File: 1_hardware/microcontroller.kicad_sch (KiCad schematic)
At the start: 42 parts, among them J1 ProgHeader, SW1 TS-1187A-B-A-B, SW2 TS-1187A-B-A-B, U1 STM32L151C8T6, X1 16MHz

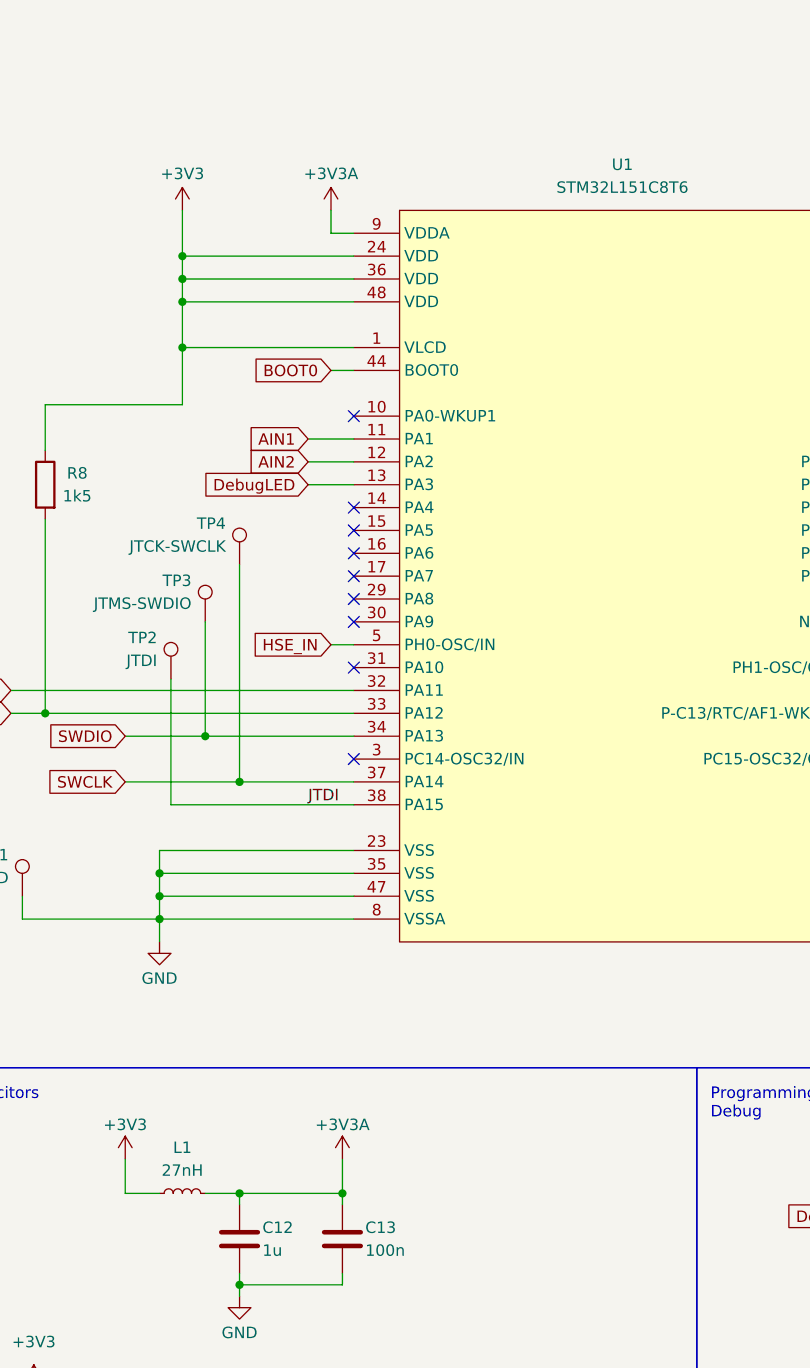
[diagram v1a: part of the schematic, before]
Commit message: PCB v0.9.4 - finished final prototype STM32 project reinitialised (F103C8 -> L151C8)
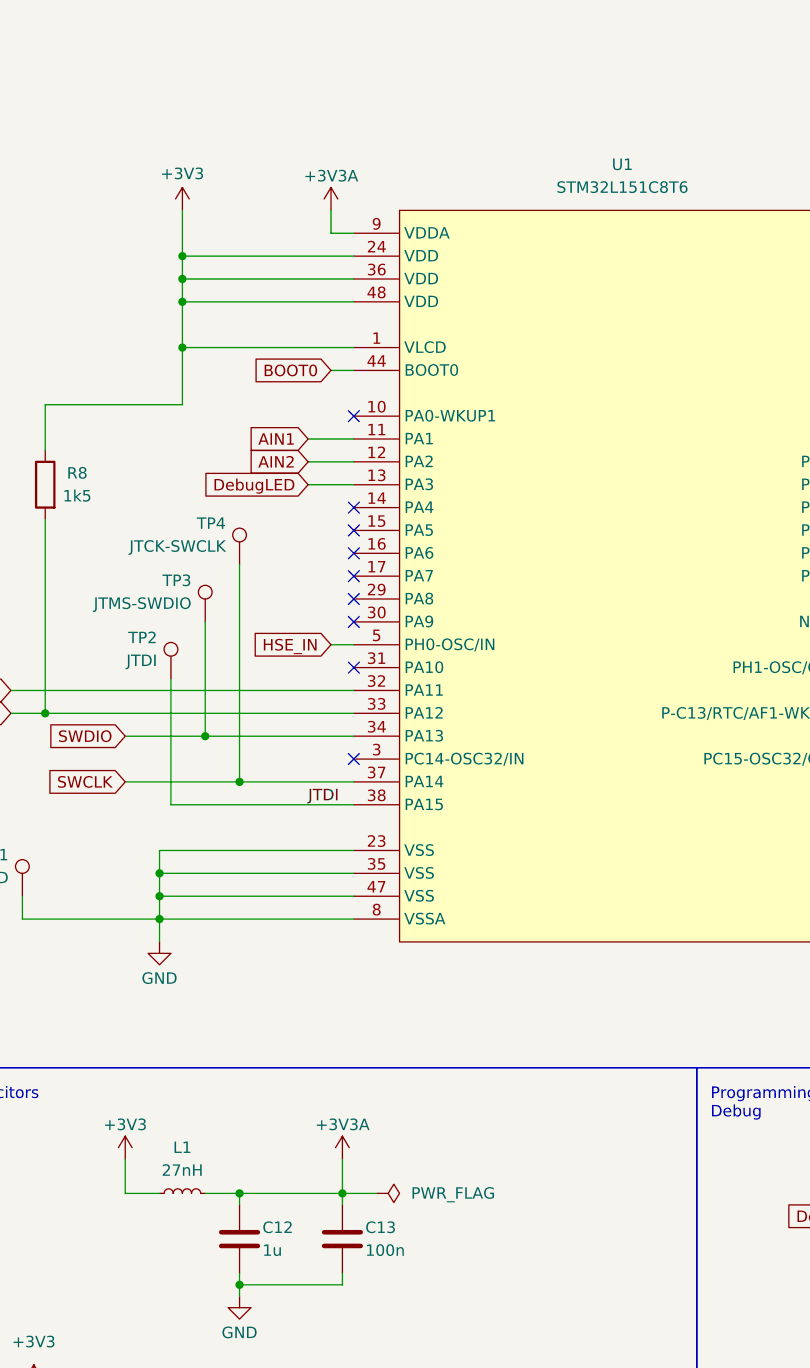
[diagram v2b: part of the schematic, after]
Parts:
- J1: footprint easyeda2kicad:HDR-SMD_6P-P2.54-V-M-LS4.8_R2 -> project_library:HDR-SMD_6P-P2.54-V-M-LS4.8_R2
- SW1, SW2: footprint easyeda2kicad:SW-SMD_4P-L5.1-W5.1-P3.70-LS6.5-TL-2 -> project_library:SW-SMD_4P-L5.1-W5.1-P3.70-LS6.5-TL-2; symbol Switch:SW_MEC_5E -> project_library:SW_MEC_5E
- U1: footprint easyeda2kicad:LQFP-48_L7.0-W7.0-P0.50-LS9.0-BL -> project_library:LQFP-48_L7.0-W7.0-P0.50-LS9.0-BL; symbol easyeda2kicad:STM32L151C8T6 -> project_library:STM32L151C8T6
- X1: footprint easyeda2kicad:CRYSTAL-SMD_4P-L3.2-W2.5-BL_SIT8008BI -> project_library:CRYSTAL-SMD_4P-L3.2-W2.5-BL_SIT8008BI; symbol easyeda2kicad:TZ0233A -> project_library:TZ0233A
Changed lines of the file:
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@@
 	(title_block
 		(title "Microcontroller logic and I2C busses")
-		(date "2024-10-18")
-		(rev "v0.9.3")
+		(date "2024-10-20")
+		(rev "v0.9.4")
 	)
 	(junction
@@
 	(wire
 		(pts
+			(xy 67.31 146.05) (xy 71.12 146.05)
+		)
+		(stroke
+			(width 0)
+			(type default)
+		)
+	)
+	(wire
+		(pts
 			(xy 267.97 33.02) (xy 259.08 33.02)
 		)
@@
 	(wire
 		(pts
+			(xy 66.04 39.37) (xy 68.58 39.37)
+		)
+		(stroke
+			(width 0)
+			(type default)
+		)
+	)
+	(wire
+		(pts
 			(xy 78.74 170.18) (xy 78.74 172.72)
 		)
@@
 	(wire
 		(pts
-			(xy 66.04 36.83) (xy 66.04 39.37)
-		)
-		(stroke
-			(width 0)
-			(type default)
-		)
-	)
-	(wire
-		(pts
 			(xy 67.31 154.94) (xy 67.31 156.21)
 		)
@@
 	(wire
 		(pts
+			(xy 66.04 36.83) (xy 66.04 39.37)
+		)
+		(stroke
+			(width 0)
+			(type default)
+		)
+	)
+	(wire
+		(pts
 			(xy 236.22 100.33) (xy 236.22 106.68)
 		)
@@
 	(wire
 		(pts
-			(xy 66.04 39.37) (xy 68.58 39.37)
-		)
-		(stroke
-			(width 0)
-			(type default)
-		)
-	)
-	(wire
-		(pts
 			(xy 133.35 59.69) (xy 128.27 59.69)
 		)
@@
 	)
 	(symbol
-		(lib_id "Switch:SW_MEC_5E")
+		(lib_id "project_library:SW_MEC_5E")
 		(at 191.77 57.15 270)
 		(unit 1)
@@
 			)
 		)
-		(property "Footprint" "easyeda2kicad:SW-SMD_4P-L5.1-W5.1-P3.70-LS6.5-TL-2"
+		(property "Footprint" "project_library:SW-SMD_4P-L5.1-W5.1-P3.70-LS6.5-TL-2"
 			(at 199.39 57.15 0)
 			(effects
@@
 			)
 		)
-		(property "Datasheet" "https://lcsc.com/product-detail/Tactile-Switches_XKB-Enterprise-TS-1187-B-A-A_C318884.html"
+		(property "Datasheet" "http://www.apem.com/int/index.php?controller=attachment&id_attachment=1371"
 			(at 199.39 57.15 0)
 			(effects
@@
 			)
 		)
-		(property "Description" ""
+		(property "Description" "MEC 5E single pole normally-open tactile switch"
 			(at 191.77 57.15 0)
 			(effects
@@
 			)
 		)
-		(property "Datasheet" "https://www.lcsc.com/product-detail/Inductors-SMD_Sunlord-SDCL1608C27NJTDF_C12100.html"
+		(property "Datasheet" "~"
 			(at 49.53 146.05 0)
 			(effects
@@
 	)
 	(symbol
-		(lib_id "power:+3V3")
-		(at 66.04 36.83 0)
-		(unit 1)
-		(exclude_from_sim no)
-		(in_bom yes)
-		(on_board yes)
-		(dnp no)
-		(property "Reference" "#PWR030"
-			(at 66.04 40.64 0)
-			(effects
-				(font
-					(size 1.27 1.27)
-				)
-				(hide yes)
-			)
-		)
-		(property "Value" "+3V3A"
-			(at 66.04 32.766 0)
-			(effects
-				(font
-					(size 1.27 1.27)
-				)
-			)
-		)
-		(property "Footprint" ""
-			(at 66.04 36.83 0)
-			(effects
-				(font
-					(size 1.27 1.27)
-				)
-				(hide yes)
-			)
-		)
-		(property "Datasheet" ""
-			(at 66.04 36.83 0)
-			(effects
-				(font
-					(size 1.27 1.27)
-				)
-				(hide yes)
-			)
-		)
-		(property "Description" "Power symbol creates a global label with name \"+3V3\""
-			(at 66.04 36.83 0)
-			(effects
-				(font
-					(size 1.27 1.27)
-				)
-				(hide yes)
-			)
-		)
-		(pin "1"
-		)
-		(instances
-			(project "Siemens-Sinumerik840C-Maschinensteuertafel-Adaptor"
-				(path "/82333ccb-6661-4401-8681-de9334259747/2cfe2c7e-83df-45dd-b60e-672a1c018e21"
-					(reference "#PWR030")
-					(unit 1)
-				)
-			)
-		)
-	)
-	(symbol
 		(lib_id "Connector:Conn_01x06_Pin")
 		(at 124.46 171.45 0)
@@
 			)
 		)
-		(property "Footprint" "easyeda2kicad:HDR-SMD_6P-P2.54-V-M-LS4.8_R2"
+		(property "Footprint" "project_library:HDR-SMD_6P-P2.54-V-M-LS4.8_R2"
 			(at 124.46 171.45 0)
 			(effects
@@
 			)
 		)
-		(property "Datasheet" "https://www.lcsc.com/product-detail/Pin-Headers_XKB-Connection-X6511WVS-06H-C60D48R2_C2883763.html"
+		(property "Datasheet" "~"
 			(at 124.46 171.45 0)
 			(effects
@@
 	)
 	(symbol
-		(lib_id "easyeda2kicad:TZ0233A")
+		(lib_id "project_library:TZ0233A")
 		(at 251.46 35.56 0)
 		(unit 1)
@@
 			)
 		)
-		(property "Footprint" "easyeda2kicad:CRYSTAL-SMD_4P-L3.2-W2.5-BL_SIT8008BI"
+		(property "Footprint" "project_library:CRYSTAL-SMD_4P-L3.2-W2.5-BL_SIT8008BI"
 			(at 251.46 45.72 0)
 			(effects
@@
 	)
 	(symbol
+		(lib_id "power:PWR_FLAG")
+		(at 71.12 146.05 270)
+		(unit 1)
+		(exclude_from_sim no)
+		(in_bom yes)
+		(on_board yes)
+		(dnp no)
+		(fields_autoplaced yes)
+		(property "Reference" "#FLG06"
+			(at 73.025 146.05 0)
+			(effects
+				(font
+					(size 1.27 1.27)
+				)
+				(hide yes)
+			)
+		)
+		(property "Value" "PWR_FLAG"
+			(at 74.93 146.0499 90)
+			(effects
+				(font
+					(size 1.27 1.27)
+				)
+				(justify left)
+			)
+		)
+		(property "Footprint" ""
+			(at 71.12 146.05 0)
+			(effects
+				(font
+					(size 1.27 1.27)
+				)
+				(hide yes)
+			)
+		)
+		(property "Datasheet" "~"
+			(at 71.12 146.05 0)
+			(effects
+				(font
+					(size 1.27 1.27)
+				)
+				(hide yes)
+			)
+		)
+		(property "Description" "Special symbol for telling ERC where power comes from"
+			(at 71.12 146.05 0)
+			(effects
+				(font
+					(size 1.27 1.27)
+				)
+				(hide yes)
+			)
+		)
+		(pin "1"
+		)
+		(instances
+			(project "Siemens-Sinumerik840C-Maschinensteuertafel-Adaptor"
+				(path "/82333ccb-6661-4401-8681-de9334259747/2cfe2c7e-83df-45dd-b60e-672a1c018e21"
+					(reference "#FLG06")
+					(unit 1)
+				)
+			)
+		)
+	)
+	(symbol
 		(lib_id "Device:R")
 		(at 255.27 88.9 180)
@@
 	)
 	(symbol
+		(lib_id "power:+3V3")
+		(at 66.04 36.83 0)
+		(unit 1)
+		(exclude_from_sim no)
+		(in_bom yes)
+		(on_board yes)
+		(dnp no)
+		(property "Reference" "#PWR030"
+			(at 66.04 40.64 0)
+			(effects
+				(font
+					(size 1.27 1.27)
+				)
+				(hide yes)
+			)
+		)
+		(property "Value" "+3V3A"
+			(at 66.04 33.02 0)
+			(effects
+				(font
+					(size 1.27 1.27)
+				)
+			)
+		)
+		(property "Footprint" ""
+			(at 66.04 36.83 0)
+			(effects
+				(font
+					(size 1.27 1.27)
+				)
+				(hide yes)
+			)
+		)
+		(property "Datasheet" ""
+			(at 66.04 36.83 0)
+			(effects
+				(font
+					(size 1.27 1.27)
+				)
+				(hide yes)
+			)
+		)
+		(property "Description" "Power symbol creates a global label with name \"+3V3\""
+			(at 66.04 36.83 0)
+			(effects
+				(font
+					(size 1.27 1.27)
+				)
+				(hide yes)
+			)
+		)
+		(pin "1"
+		)
+		(instances
+			(project "Siemens-Sinumerik840C-Maschinensteuertafel-Adaptor"
+				(path "/82333ccb-6661-4401-8681-de9334259747/2cfe2c7e-83df-45dd-b60e-672a1c018e21"
+					(reference "#PWR030")
+					(unit 1)
+				)
+			)
+		)
+	)
+	(symbol
 		(lib_id "power:GND")
 		(at 46.99 118.11 0)
@@
 	)
 	(symbol
-		(lib_id "easyeda2kicad:STM32L151C8T6")
+		(lib_id "project_library:STM32L151C8T6")
 		(at 99.06 77.47 0)
 		(unit 1)
@@
 			)
 		)
-		(property "Footprint" "easyeda2kicad:LQFP-48_L7.0-W7.0-P0.50-LS9.0-BL"
+		(property "Footprint" "project_library:LQFP-48_L7.0-W7.0-P0.50-LS9.0-BL"
 			(at 99.06 123.19 0)
 			(effects
@@
 	)
 	(symbol
-		(lib_id "Switch:SW_MEC_5E")
+		(lib_id "project_library:SW_MEC_5E")
 		(at 191.77 113.03 270)
 		(unit 1)
@@
 			)
 		)
-		(property "Footprint" "easyeda2kicad:SW-SMD_4P-L5.1-W5.1-P3.70-LS6.5-TL-2"
+		(property "Footprint" "project_library:SW-SMD_4P-L5.1-W5.1-P3.70-LS6.5-TL-2"
 			(at 199.39 113.03 0)
 			(effects
@@
 			)
 		)
-		(property "Datasheet" "https://lcsc.com/product-detail/Tactile-Switches_XKB-Enterprise-TS-1187-B-A-A_C318884.html"
+		(property "Datasheet" "http://www.apem.com/int/index.php?controller=attachment&id_attachment=1371"
 			(at 199.39 113.03 0)
 			(effects
@@
 			)
 		)
-		(property "Description" ""
+		(property "Description" "MEC 5E single pole normally-open tactile switch"
 			(at 191.77 113.03 0)
 			(effects

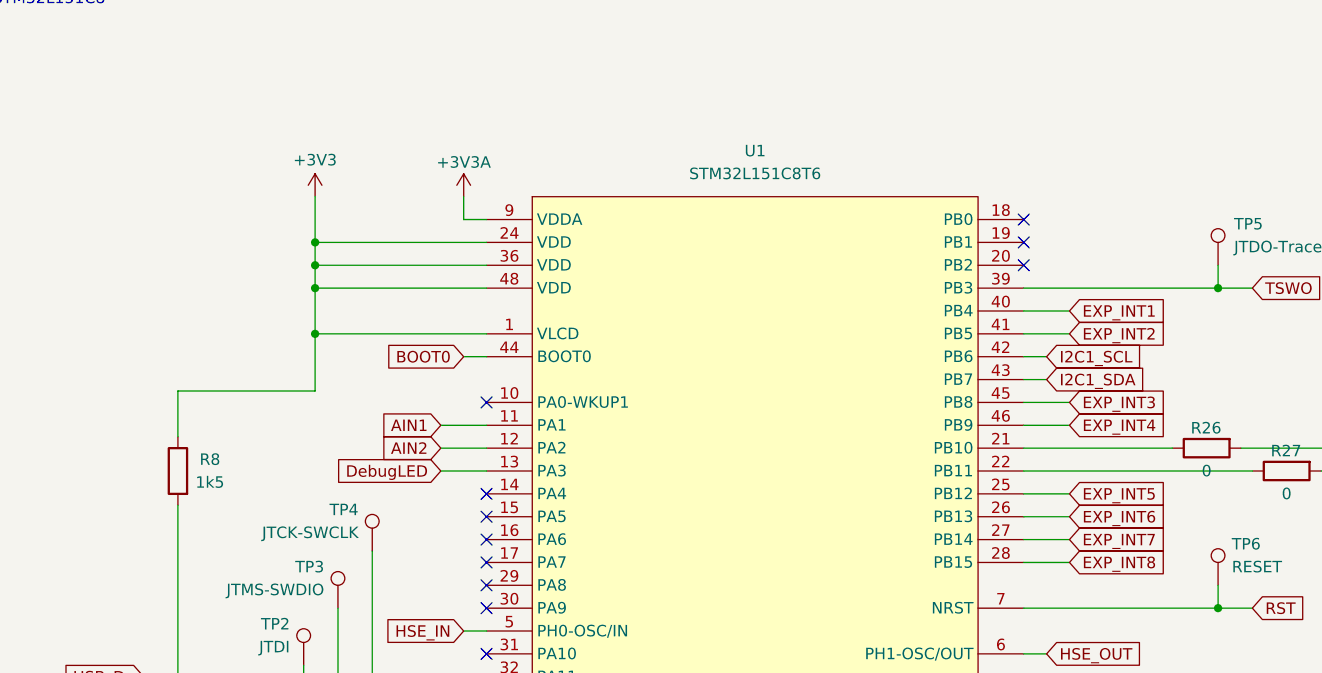
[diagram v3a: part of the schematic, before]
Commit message: started with PCB v0.9.6, software WIP communication with expander working, able to read inputs and set outputs, matrix for properly key-mapping and serial still needs to be done bugs from first badge of boards need to be fixed for version v1.0 -> (upcoming) changelog for v0.9.6  - PullUp Resistor on USB+ not needed  - for DFU to be working, BOOT1 (PB2) needs to be tied to GND  - second I2C bus not needed -> will be combined into one  - ...
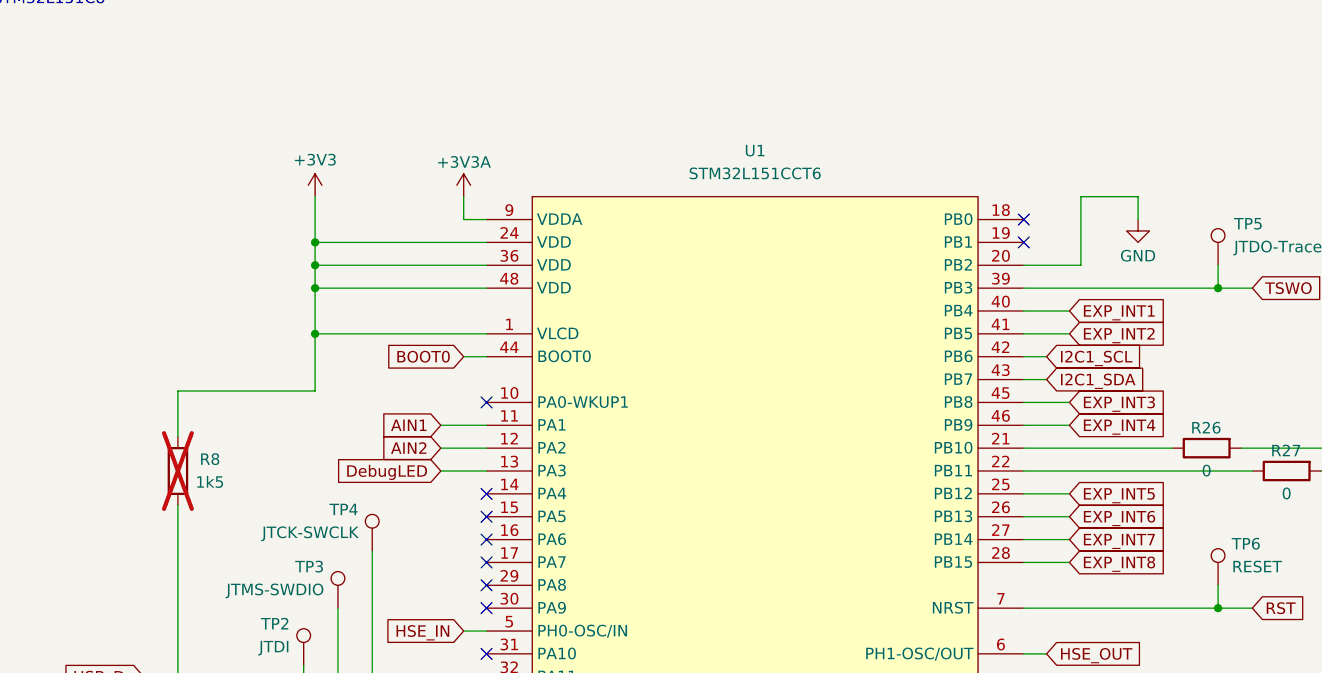
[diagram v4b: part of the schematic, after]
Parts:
- R8: now not fitted
- U1: value STM32L151C8T6 -> STM32L151CCT6; LCSC Part C9861 -> C2149675
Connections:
- net GND: now also U1.20 (PB2)
- no-connect marks 14 -> 13
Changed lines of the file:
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@@
 	(title_block
 		(title "Microcontroller logic and I2C busses")
-		(date "2024-10-27")
-		(rev "v0.9.5")
+		(date "2024-12-09")
+		(rev "v0.9.6")
 	)
 	(junction
@@
 	)
 	(no_connect
-		(at 128.27 44.45)
-	)
-	(no_connect
 		(at 68.58 87.63)
 	)
@@
 	(wire
 		(pts
+			(xy 134.62 44.45) (xy 128.27 44.45)
+		)
+		(stroke
+			(width 0)
+			(type default)
+		)
+	)
+	(wire
+		(pts
 			(xy 52.07 146.05) (xy 55.88 146.05)
 		)
@@
 	(wire
 		(pts
+			(xy 134.62 36.83) (xy 134.62 44.45)
+		)
+		(stroke
+			(width 0)
+			(type default)
+		)
+	)
+	(wire
+		(pts
 			(xy 34.29 92.71) (xy 68.58 92.71)
 		)
@@
 	(wire
 		(pts
+			(xy 140.97 39.37) (xy 140.97 36.83)
+		)
+		(stroke
+			(width 0)
+			(type default)
+		)
+	)
+	(wire
+		(pts
+			(xy 140.97 36.83) (xy 134.62 36.83)
+		)
+		(stroke
+			(width 0)
+			(type default)
+		)
+	)
+	(wire
+		(pts
 			(xy 259.08 92.71) (xy 259.08 82.55)
 		)
@@
 	)
 	(symbol
+		(lib_id "power:GND")
+		(at 140.97 39.37 0)
+		(unit 1)
+		(exclude_from_sim no)
+		(in_bom yes)
+		(on_board yes)
+		(dnp no)
+		(property "Reference" "#PWR026"
+			(at 140.97 45.72 0)
+			(effects
+				(font
+					(size 1.27 1.27)
+				)
+				(hide yes)
+			)
+		)
+		(property "Value" "GND"
+			(at 140.97 43.434 0)
+			(effects
+				(font
+					(size 1.27 1.27)
+				)
+			)
+		)
+		(property "Footprint" ""
+			(at 140.97 39.37 0)
+			(effects
+				(font
+					(size 1.27 1.27)
+				)
+				(hide yes)
+			)
+		)
+		(property "Datasheet" ""
+			(at 140.97 39.37 0)
+			(effects
+				(font
+					(size 1.27 1.27)
+				)
+				(hide yes)
+			)
+		)
+		(property "Description" "Power symbol creates a global label with name \"GND\" , ground"
+			(at 140.97 39.37 0)
+			(effects
+				(font
+					(size 1.27 1.27)
+				)
+				(hide yes)
+			)
+		)
+		(pin "1"
+		)
+		(instances
+			(project "Siemens-Sinumerik840C-Maschinensteuertafel-Adaptor"
+				(path "/82333ccb-6661-4401-8681-de9334259747/2cfe2c7e-83df-45dd-b60e-672a1c018e21"
+					(reference "#PWR026")
+					(unit 1)
+				)
+			)
+		)
+	)
+	(symbol
 		(lib_id "Device:R")
 		(at 237.49 139.7 180)
@@
 		(in_bom yes)
 		(on_board yes)
-		(dnp no)
+		(dnp yes)
 		(property "Reference" "R8"
 			(at 37.846 66.04 0)
@@
 			)
 		)
-		(property "Value" "STM32L151C8T6"
+		(property "Value" "STM32L151CCT6"
 			(at 98.425 34.29 0)
 			(effects
@@
 			)
 		)
-		(property "Datasheet" "https://lcsc.com/product-detail/ST-Microelectronics_STMicroelectronics_STM32L151C8T6_STM32L151C8T6_C9861.html"
+		(property "Datasheet" "https://www.lcsc.com/product-detail/Microcontrollers-MCU-MPU-SOC_STMicroelectronics-STM32L151CCT6_C2149675.html"
 			(at 99.06 125.73 0)
 			(effects
@@
 			)
 		)
-		(property "LCSC Part" "C9861"
+		(property "LCSC Part" "C2149675"
 			(at 99.06 128.27 0)
 			(effects
